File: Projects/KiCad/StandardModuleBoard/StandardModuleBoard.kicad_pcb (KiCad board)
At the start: 2 copper layers, 120 x 105 mm, 13 parts, among them J1 Conn_01x04_Male, J2 Conn_01x04_Female, U1 MCP2562-E-P, U2 NUCLEO-F303K8

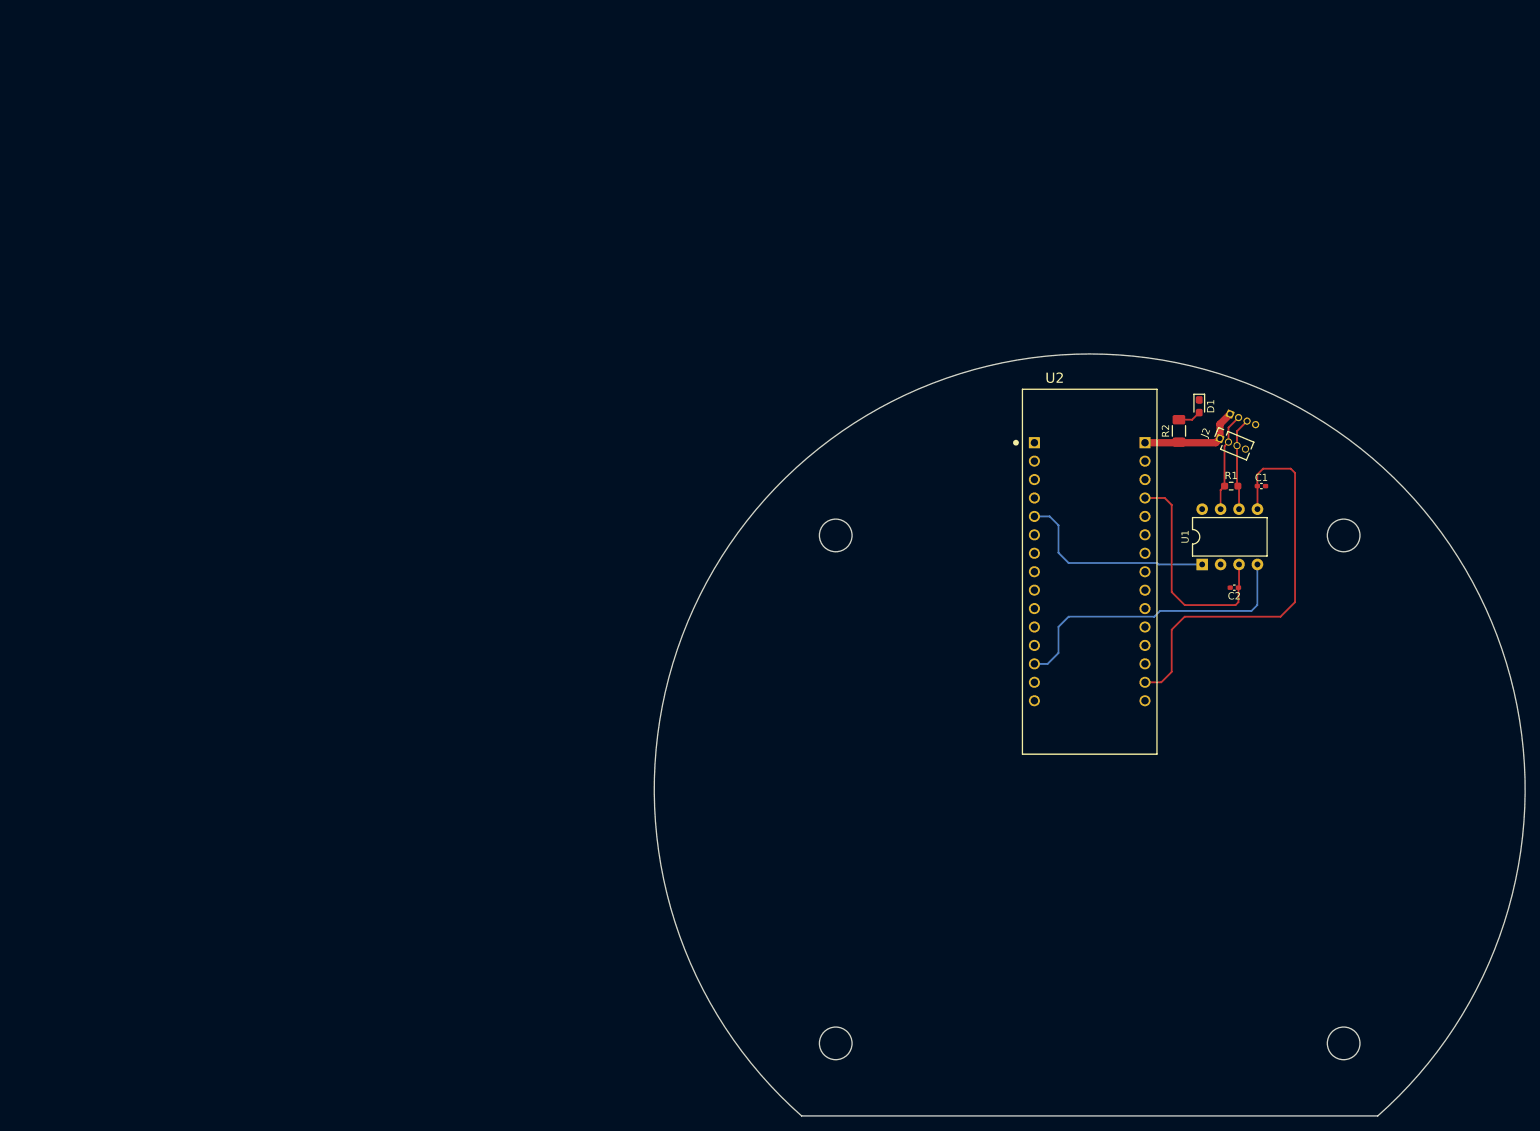
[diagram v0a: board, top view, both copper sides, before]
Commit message: 標準モジュール基板の回路図を修正
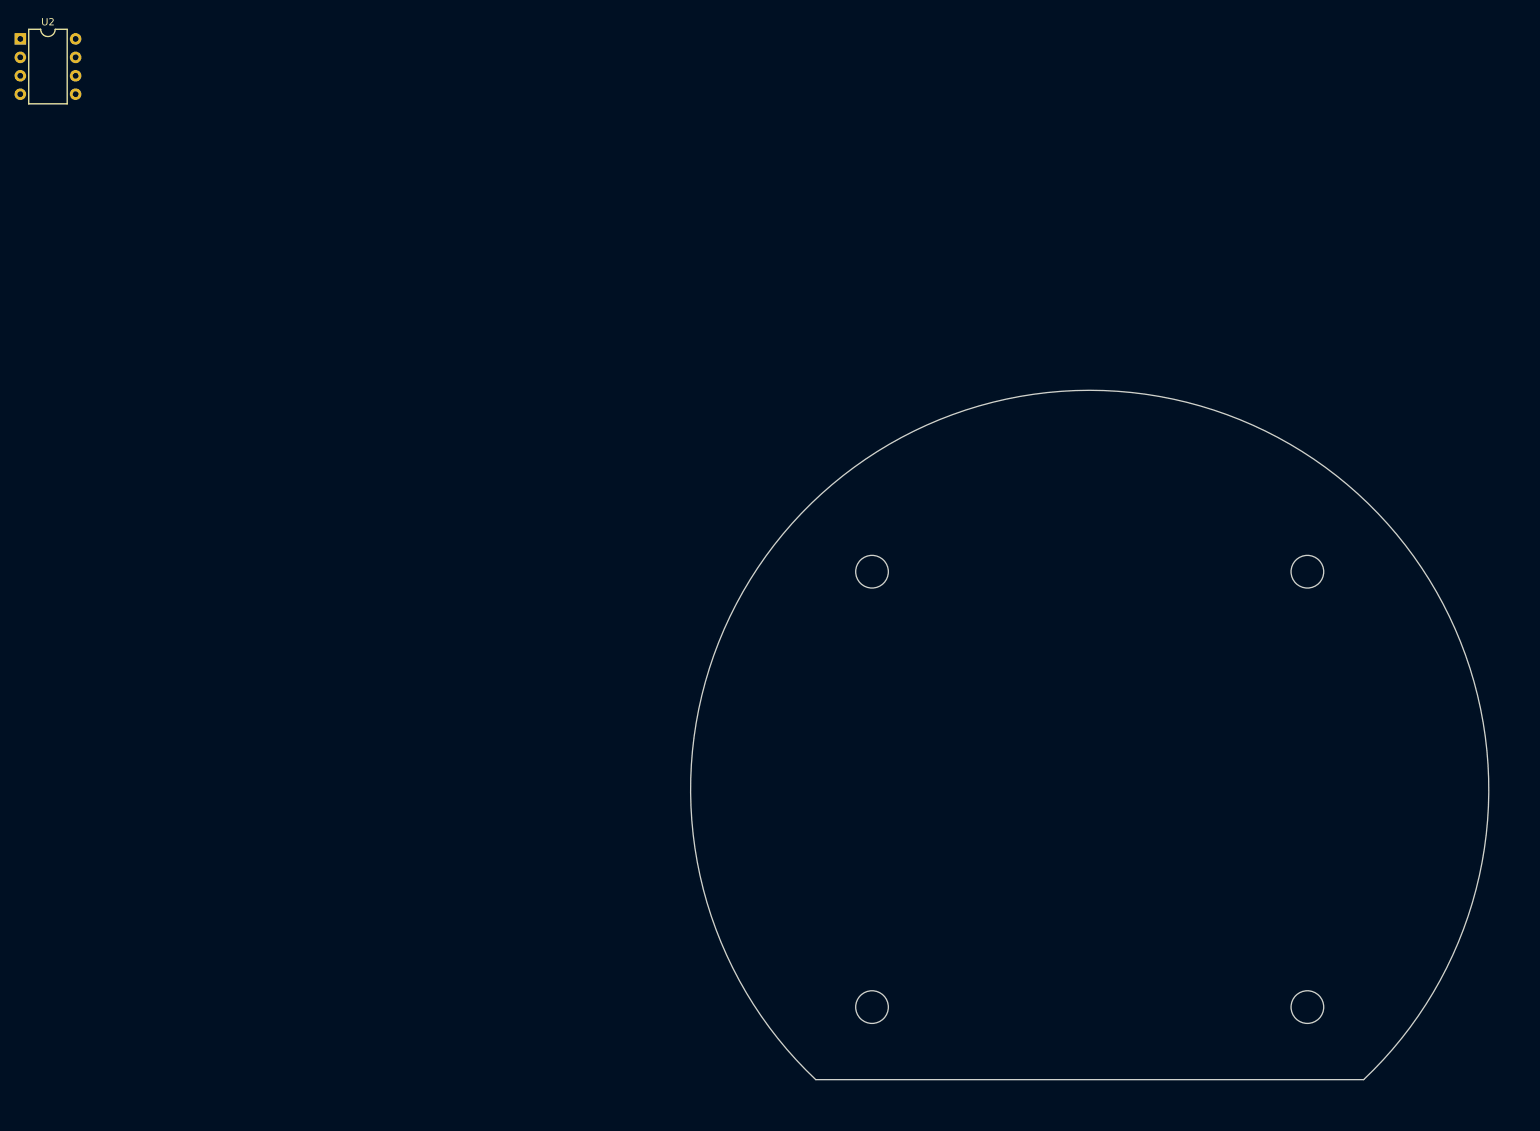
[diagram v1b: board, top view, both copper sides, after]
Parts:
- removed C1, C2: C, Capacitor_SMD:C_0402_1005Metric_Pad0.74x0.62mm_HandSolder
- removed D1: LED, LED_SMD:LED_0603_1608Metric_Pad1.05x0.95mm_HandSolder
- removed J1: Conn_01x04_Male, Connector_PinHeader_1.27mm:PinHeader_1x04_P1.27mm_Vertical
- removed J2: Conn_01x04_Female, Connector_PinSocket_1.27mm:PinSocket_1x04_P1.27mm_Vertical
- removed R1: 120R, Resistor_SMD:R_0603_1608Metric_Pad0.98x0.95mm_HandSolder
- removed R2: R, Resistor_SMD:R_1206_3216Metric_Pad1.30x1.75mm_HandSolder
- removed the REF** at (183.5, 140.0)
- removed the REF** at (113.5, 140.0)
- removed the REF** at (183.5, 70.0)
- removed the REF** at (113.5, 70.0)
- removed U1: MCP2562-E-P, Package_DIP:DIP-8_W7.62mm
- added REF**: MountingHole_4.5mm, MountingHole:MountingHole_4.5mm, F.Cu at (178.5, 75.0)
- added REF**: MountingHole_4.5mm, MountingHole:MountingHole_4.5mm, F.Cu at (178.5, 135.0)
- added REF**: MountingHole_4.5mm, MountingHole:MountingHole_4.5mm, F.Cu at (118.5, 75.0)
- added REF**: MountingHole_4.5mm, MountingHole:MountingHole_4.5mm, F.Cu at (118.5, 135.0)
- U2: value NUCLEO-F303K8 -> MCP2562-E-P; footprint NUCLEO-F303K8:MODULE_NUCLEO-F303K8 -> Package_DIP:DIP-8_W7.62mm
- moved U2 164.7 mm to (1.12, 1.57)
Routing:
- net +3.3V: track 57.0 -> 0.00 mm
- net Net-(U1-Pad4): track 41.8 -> 0.00 mm
- net +5V: track 31.4 -> 0.00 mm
- net Net-(U1-Pad1): track 28.1 -> 0.00 mm
- net +12V: track 14.5 -> 0.00 mm
- net Net-(U1-Pad7): track 13.6 -> 0.00 mm
- net Net-(J1-Pad3): track 12.8 -> 0.00 mm
- net Net-(D1-Pad2): track 3.20 -> 0.00 mm
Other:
- board size 120 x 105 mm -> 110 x 95 mm

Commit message: 標準モジュール基板のボード図を修正
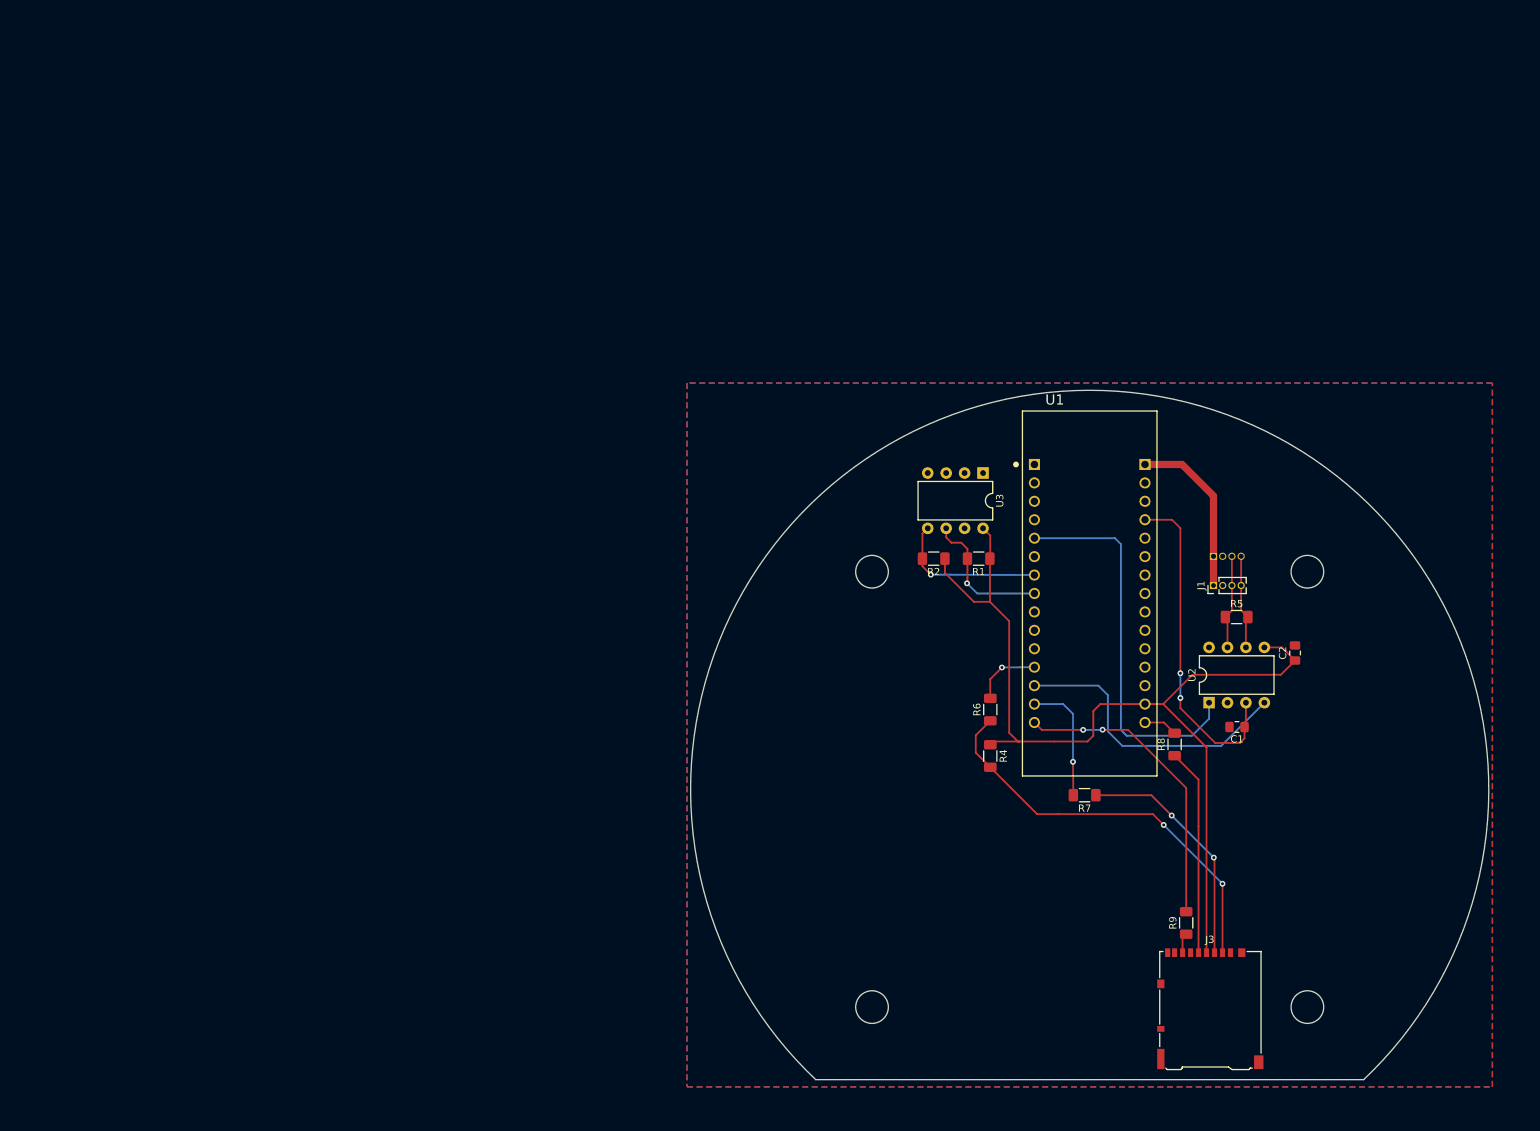
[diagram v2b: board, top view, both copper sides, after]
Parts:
- added C1: 0.1μF, Capacitor_SMD:C_0805_2012Metric_Pad1.18x1.45mm_HandSolder, F.Cu at (168.8, 96.4)
- added C2: 0.1μF, Capacitor_SMD:C_0805_2012Metric_Pad1.18x1.45mm_HandSolder, F.Cu at (176.8, 86.2)
- added J1: Conn_01x04_Pin, Connector_PinHeader_1.27mm:PinHeader_1x04_P1.27mm_Vertical, F.Cu at (165.6, 76.9)
- added J2: Conn_01x04_Socket, Connector_PinSocket_1.27mm:PinSocket_1x04_P1.27mm_Vertical, B.Cu at (165.6, 72.9)
- added J3: Micro_SD_Card_Det_Hirose_DM3AT, Connector_Card:microSD_HC_Hirose_DM3AT-SF-PEJM5, F.Cu at (165.1, 135.2)
- added R1: 2.2kΩ, Resistor_SMD:R_1206_3216Metric_Pad1.30x1.75mm_HandSolder, F.Cu at (133.2, 73.2)
- added R2: 2.2kΩ, Resistor_SMD:R_1206_3216Metric_Pad1.30x1.75mm_HandSolder, F.Cu at (127.0, 73.2)
- added R4: 4.7kΩ, Resistor_SMD:R_1206_3216Metric_Pad1.30x1.75mm_HandSolder, F.Cu at (134.8, 100.4)
- added R5: 120R1/4W, Resistor_SMD:R_1206_3216Metric_Pad1.30x1.75mm_HandSolder, F.Cu at (168.8, 81.2)
- added R6: 22Ω, Resistor_SMD:R_1206_3216Metric_Pad1.30x1.75mm_HandSolder, F.Cu at (134.8, 94.0)
- added R7: 22Ω, Resistor_SMD:R_1206_3216Metric_Pad1.30x1.75mm_HandSolder, F.Cu at (147.8, 105.8)
- added R8: 22Ω, Resistor_SMD:R_1206_3216Metric_Pad1.30x1.75mm_HandSolder, F.Cu at (160.2, 98.8)
- added R9: 22Ω, Resistor_SMD:R_1206_3216Metric_Pad1.30x1.75mm_HandSolder, F.Cu at (161.8, 123.4)
- added U1: NUCLEO-F303K8, NUCLEO-F303K8:MODULE_NUCLEO-F303K8, F.Cu at (148.5, 78.0)
- added U3: 24LC256, Package_DIP:DIP-8_W7.62mm, F.Cu at (133.8, 61.4)
- moved U2 187.6 mm to (164.9, 93.0), turned to 90 degrees
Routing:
- net +3.3V: track 0.00 -> 131.9 mm
- net SPI_CS_SD: track 0.00 -> 56.2 mm, vias 0 -> 2
- net CAN_TX: track 0.00 -> 53.5 mm
- net +5V: track 0.00 -> 46.2 mm, vias 0 -> 2
- net SPI_MISO: track 0.00 -> 41.7 mm, vias 0 -> 2
- net CAN_RX: track 0.00 -> 40.5 mm
- net SPI_MOSI: track 0.00 -> 33.1 mm, vias 0 -> 2
- net SPI_SCLK: track 0.00 -> 28.5 mm
- net +12V: track 0.00 -> 23.6 mm
- net I2C_SDA: track 0.00 -> 21.5 mm, vias 0 -> 1
- net I2C_SCL: track 0.00 -> 19.5 mm, vias 0 -> 1
- net Net-(U1A-PB5): track 0.00 -> 17.2 mm, vias 0 -> 1
- net CAN_L: track 0.00 -> 13.1 mm
- net CAN_H: track 0.00 -> 13.0 mm
- net Net-(U1A-PA8): track 0.00 -> 9.45 mm, vias 0 -> 1
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- added copper zone on B.Cu, net GND
- added copper zone on F.Cu, net GND

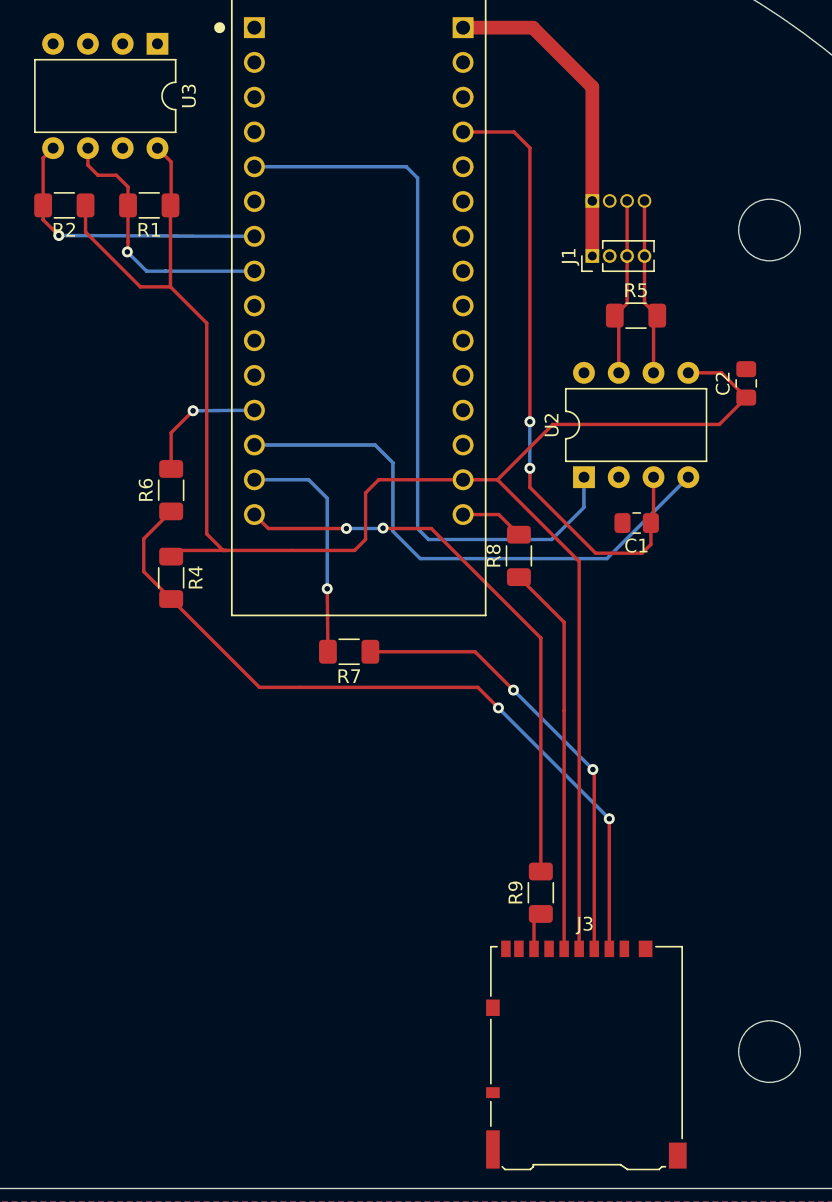
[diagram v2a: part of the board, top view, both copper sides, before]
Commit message: 標準モジュール基板のボード図をいい感じに変更
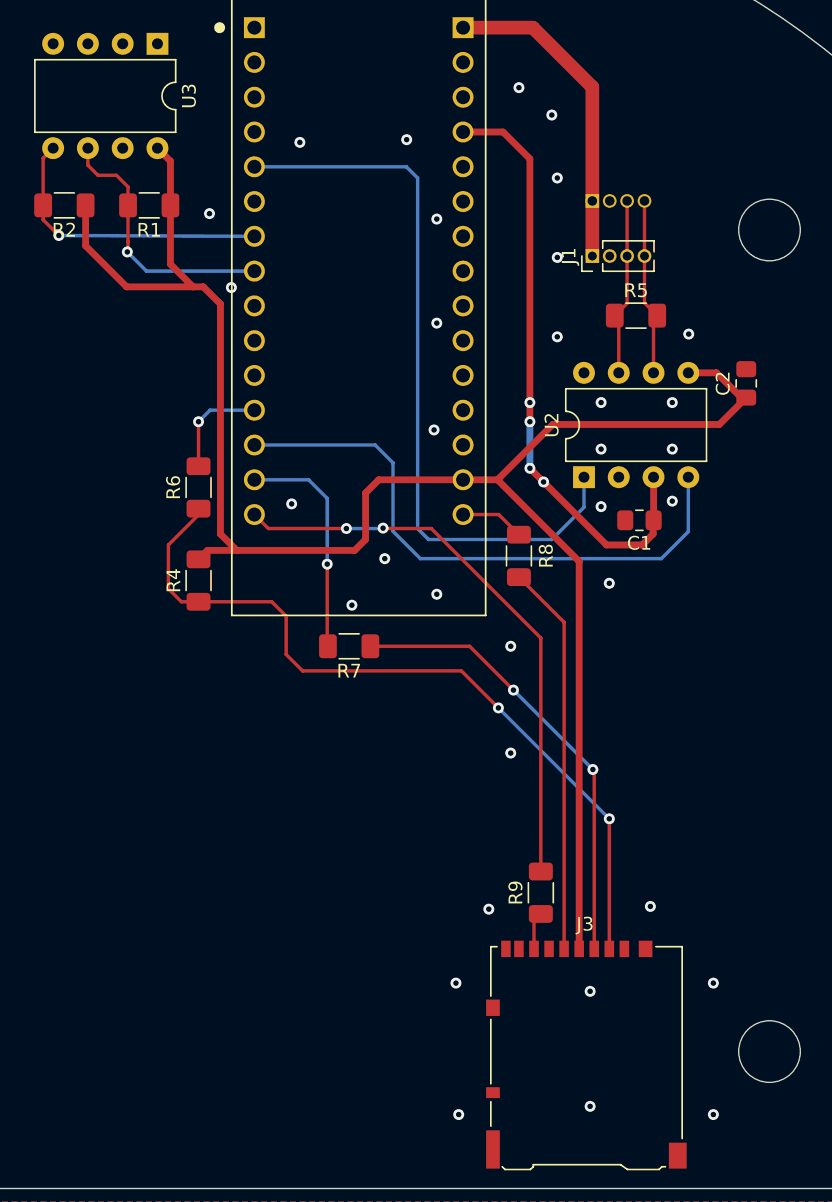
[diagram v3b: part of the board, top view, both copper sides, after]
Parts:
- moved R6 2.01 mm to (136.8, 93.8)
- moved R4 2.01 mm to (136.8, 100.6)
- moved R7 0.40 mm to (147.8, 105.4)
- moved C1 0.28 mm to (169.0, 96.2)
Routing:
- net CAN_RX: track 40.5 -> 42.9 mm
- net +5V: track 46.2 -> 44.1 mm, vias 2 -> 4
- net Net-(U1A-PA8): track 9.45 -> 7.68 mm
- net +3.3V: track 131.9 -> 132.9 mm
- net SPI_CS_SD: track 56.2 -> 57.1 mm
- net GND: vias 0 -> 34
